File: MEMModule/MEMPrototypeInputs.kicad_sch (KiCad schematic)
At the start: 6 parts, among them J2 PC, J3 Y_MEM, J4 StoreOp_MEM, J5 Ctl_MEM, J6 SelC_MEM, J7 Control Signals

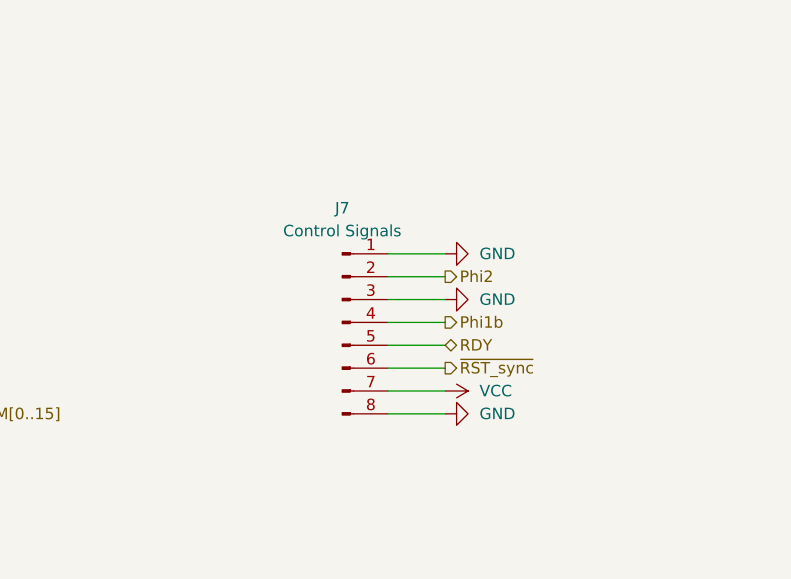
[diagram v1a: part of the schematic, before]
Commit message: MEMModule: Add FLUSH_IF input
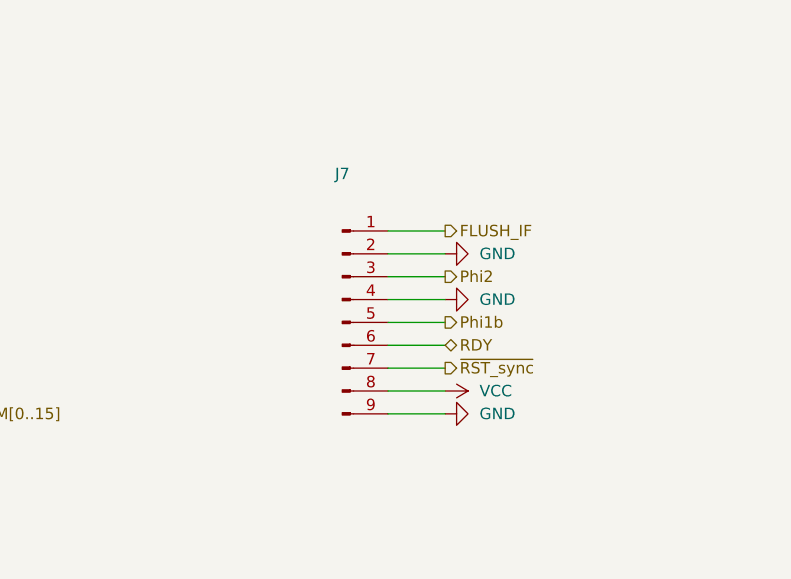
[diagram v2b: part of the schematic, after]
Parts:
- J7: value Control Signals -> (none); footprint Connector_PinHeader_2.54mm:PinHeader_1x08_P2.54mm_Vertical -> (none); symbol Connector:Conn_01x08_Male -> Connector:Conn_01x09_Male
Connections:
- net GND: now also J7.2 (Pin_2), J7.4 (Pin_4), J7.9 (Pin_9); no longer J7.1 (Pin_1), J7.3 (Pin_3), J7.8 (Pin_8)
- net Phi1b: now also J7.5 (Pin_5); no longer J7.4 (Pin_4)
- net Phi2: now also J7.3 (Pin_3); no longer J7.2 (Pin_2)
- net RDY: now also J7.6 (Pin_6); no longer J7.5 (Pin_5)
- net VCC: now also J7.8 (Pin_8); no longer J7.7 (Pin_7)
- net ~{RST_sync}: now also J7.7 (Pin_7); no longer J7.6 (Pin_6)
- new net FLUSH_IF: J7.1 (Pin_1)
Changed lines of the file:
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@@
+    (stroke (width 0) (type default) (color 0 0 0 0))
+  )
+  (wire (pts (xy 179.07 128.27) (xy 185.42 128.27))
     (stroke (width 0) (type default) (color 0 0 0 0))
   )
@@
   )
   (hierarchical_label "Phi2" (shape output) (at 185.42 133.35 0)
+    (effects (font (size 1.27 1.27)) (justify left))
+  )
+  (hierarchical_label "FLUSH_IF" (shape output) (at 185.42 128.27 0)
     (effects (font (size 1.27 1.27)) (justify left))
   )
@@
     (pin "1")
   )
-  (symbol (lib_id "Connector:Conn_01x08_Male") (at 173.99 138.43 0) (unit 1)
+  (symbol (lib_id "Connector:Conn_01x09_Male") (at 173.99 138.43 0) (unit 1)
     (in_bom yes) (on_board yes)
-    (property "Reference" "J7" (id 0) (at 173.99 125.73 0))
-    (property "Value" "Control Signals" (id 1) (at 173.99 128.27 0))
-    (property "Footprint" "Connector_PinHeader_2.54mm:PinHeader_1x08_P2.54mm_Vertical" (id 2) (at 173.99 138.43 0)
+    (property "Reference" "J7" (id 0) (at 173.99 121.92 0))
+    (property "Value" "" (id 1) (at 173.99 124.46 0))
+    (property "Footprint" "" (id 2) (at 173.99 138.43 0)
       (effects (font (size 1.27 1.27)) hide)
     )
@@
     (pin "7")
     (pin "8")
+    (pin "9")
   )
   (symbol (lib_id "Connector:Conn_01x16_Male") (at 96.52 171.45 0) (unit 1)

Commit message: MEMModule now has ROM on Bank 0 again
The idea of having a system with no built-in ROM is turning out to be more
complicated than I expected. The boot device is additional complexity that
I'm now reluctant to take on. It's still, after months, not fully designed
and prototyped. Let's eliminate the need for this entire module by having
the computer run from ROM on boot.

The benefits of a ROM-less system are more difficult to achieve than
expected. The device would need a fast sixteen bit ALU chip as in the
program counter. Using simple counters like the 74F161 would bottleneck the
counting sopeed at 12.5MHz and the boot device provides no effective speed
benefit.

Further, the entire scheme is a performance optimization for a machine that
hasn't even been fully constructed yet. I can take on optimization work
later.

So this change sticks a pair of fast ROMS into MEM on Bank zero. A program
can set the Bank register to something else in order to map the built-in
RAM to instruction memory instead.

Also, update MEMModule for KiCad 7.
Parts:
- J2, J3, J4: symbol Connector:Conn_01x16_Male -> Connector:Conn_01x16_Pin
- J5: symbol Connector:Conn_01x07_Male -> Connector:Conn_01x07_Pin
- J6: symbol Connector:Conn_01x03_Male -> Connector:Conn_01x03_Pin
- J7: value (none) -> Control Signals; footprint (none) -> Connector_PinHeader_2.54mm:PinHeader_1x09_P2.54mm_Vertical; symbol Connector:Conn_01x09_Male -> Connector:Conn_01x09_Pin
